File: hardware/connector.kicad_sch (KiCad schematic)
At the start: 6 parts, among them J1 SAFETY_SUPPLY, J2 SWDIO_CONN, J3 SENSORS, J4 VALVES, J5 MAIN, J6 IDC Connector

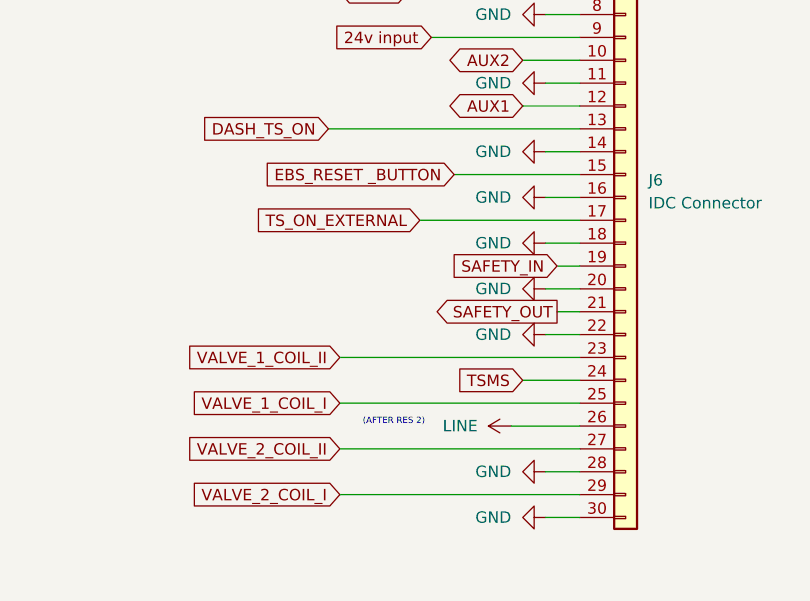
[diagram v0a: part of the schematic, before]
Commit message: replace RES2 input to actuator relai
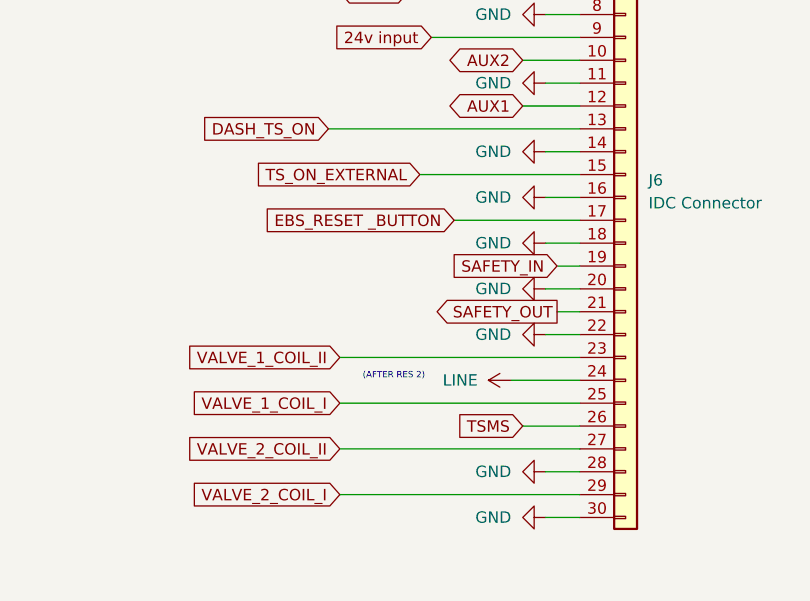
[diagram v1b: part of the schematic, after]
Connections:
- net EBS_RESET _BUTTON: now also J6.17 (Pin_17); no longer J6.15 (Pin_15)
- net LINE: now also J6.24 (Pin_24); no longer J6.26 (Pin_26)
- net TSMS: now also J6.26 (Pin_26); no longer J6.24 (Pin_24)
- net TS_ON_EXTERNAL: now also J6.15 (Pin_15); no longer J6.17 (Pin_17)
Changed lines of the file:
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@@
-    (stroke (width 0) (type default))
-  )
-  (wire (pts (xy 241.3 114.3) (xy 248.92 114.3))
     (stroke (width 0) (type default))
   )
@@
     (stroke (width 0) (type default))
   )
-  (wire (pts (xy 234.95 86.36) (xy 248.92 86.36))
-    (stroke (width 0) (type default))
-  )
-  (wire (pts (xy 231.14 91.44) (xy 248.92 91.44))
-    (stroke (width 0) (type default))
-  )
   (wire (pts (xy 245.11 99.06) (xy 248.92 99.06))
     (stroke (width 0) (type default))
@@
     (stroke (width 0) (type default))
   )
+  (wire (pts (xy 242.57 114.3) (xy 248.92 114.3))
+    (stroke (width 0) (type default))
+  )
   (wire (pts (xy 248.92 81.28) (xy 220.98 81.28))
     (stroke (width 0) (type default))
@@
     (stroke (width 0) (type default))
   )
+  (wire (pts (xy 231.14 86.36) (xy 248.92 86.36))
+    (stroke (width 0) (type default))
+  )
   (wire (pts (xy 245.11 68.58) (xy 248.92 68.58))
     (stroke (width 0) (type default))
@@
     (stroke (width 0) (type default))
   )
-  (wire (pts (xy 242.57 109.22) (xy 248.92 109.22))
+  (wire (pts (xy 241.3 109.22) (xy 248.92 109.22))
     (stroke (width 0) (type default))
   )
@@
   )
   (polyline (pts (xy 143.51 62.23) (xy 143.51 63.5))
+    (stroke (width 0) (type default))
+  )
+  (wire (pts (xy 234.95 91.44) (xy 248.92 91.44))
     (stroke (width 0) (type default))
   )
@@
   (text "HARWIN J-TEK\n" (at 158.75 92.71 0)
     (effects (font (size 1.27 1.27)) (justify left bottom))
-  )
-  (text "(AFTER RES 2)" (at 224.79 114.3 0)
-    (effects (font (size 0.7 0.7)) (justify left bottom))
   )
   (text "Connectors are divided intentionaly- Clue is to speed up inspection process where scrutineer will be unplugging different things and checking functional safety of the system\n"
     (at 49.53 146.05 0)
     (effects (font (size 1.27 1.27) italic) (justify left bottom))
+  )
+  (text "(AFTER RES 2)" (at 224.79 109.22 0)
+    (effects (font (size 0.7 0.7)) (justify left bottom))
   )
   (text "\nM80-5L11242MC\n" (at 161.29 125.73 0)
@@
     )
   )
-  (global_label "EBS_RESET _BUTTON" (shape input) (at 234.95 86.36 180) (fields_autoplaced)
-    (effects (font (size 1.27 1.27)) (justify right))
-    (property "Intersheetrefs" "${INTERSHEET_REFS}" (at 213.0636 86.4394 0)
+  (global_label "TSMS" (shape input) (at 242.57 114.3 180) (fields_autoplaced)
+    (effects (font (size 1.27 1.27)) (justify right))
+    (property "Intersheetrefs" "${INTERSHEET_REFS}" (at 234.8262 114.3 0)
       (effects (font (size 1.27 1.27)) (justify right) hide)
     )
@@
     )
   )
+  (global_label "EBS_RESET _BUTTON" (shape input) (at 234.95 91.44 180) (fields_autoplaced)
+    (effects (font (size 1.27 1.27)) (justify right))
+    (property "Intersheetrefs" "${INTERSHEET_REFS}" (at 213.0636 91.5194 0)
+      (effects (font (size 1.27 1.27)) (justify right) hide)
+    )
+  )
   (global_label "SAFETY_IN" (shape input) (at 246.38 96.52 180) (fields_autoplaced)
     (effects (font (size 1.27 1.27)) (justify right))
@@
     (effects (font (size 1.27 1.27)) (justify right))
     (property "Intersheetrefs" "${INTERSHEET_REFS}" (at 202.7738 53.34 0)
+      (effects (font (size 1.27 1.27)) (justify right) hide)
+    )
+  )
+  (global_label "TS_ON_EXTERNAL" (shape input) (at 231.14 86.36 180) (fields_autoplaced)
+    (effects (font (size 1.27 1.27)) (justify right))
+    (property "Intersheetrefs" "${INTERSHEET_REFS}" (at 212.7612 86.4394 0)
       (effects (font (size 1.27 1.27)) (justify right) hide)
     )
@@
     (effects (font (size 1.27 1.27)) (justify right))
     (property "Intersheetrefs" "${INTERSHEET_REFS}" (at 235.3188 78.6606 0)
-      (effects (font (size 1.27 1.27)) (justify right) hide)
-    )
-  )
-  (global_label "TSMS" (shape input) (at 242.57 109.22 180) (fields_autoplaced)
-    (effects (font (size 1.27 1.27)) (justify right))
-    (property "Intersheetrefs" "${INTERSHEET_REFS}" (at 234.8262 109.22 0)
-      (effects (font (size 1.27 1.27)) (justify right) hide)
-    )
-  )
-  (global_label "TS_ON_EXTERNAL" (shape input) (at 231.14 91.44 180) (fields_autoplaced)
-    (effects (font (size 1.27 1.27)) (justify right))
-    (property "Intersheetrefs" "${INTERSHEET_REFS}" (at 212.7612 91.5194 0)
       (effects (font (size 1.27 1.27)) (justify right) hide)
     )
@@
     )
   )
-  (symbol (lib_id "power:LINE") (at 241.3 114.3 90) (unit 1)
+  (symbol (lib_id "power:LINE") (at 241.3 109.22 90) (unit 1)
     (in_bom yes) (on_board yes) (dnp no)
-    (property "Reference" "#PWR073" (at 245.11 114.3 0)
-      (effects (font (size 1.27 1.27)) hide)
-    )
-    (property "Value" "LINE" (at 233.68 114.3 90)
+    (property "Reference" "#PWR017" (at 245.11 109.22 0)
+      (effects (font (size 1.27 1.27)) hide)
+    )
+    (property "Value" "LINE" (at 233.68 109.22 90)
       (effects (font (size 1.27 1.27)) (justify right))
     )
-    (property "Footprint" "" (at 241.3 114.3 0)
-      (effects (font (size 1.27 1.27)) hide)
-    )
-    (property "Datasheet" "" (at 241.3 114.3 0)
+    (property "Footprint" "" (at 241.3 109.22 0)
+      (effects (font (size 1.27 1.27)) hide)
+    )
+    (property "Datasheet" "" (at 241.3 109.22 0)
       (effects (font (size 1.27 1.27)) hide)
     )
@@
       (project "PUTM_DV_EBS_2023"
         (path "/d921fbb5-521e-405d-bdec-f40195adfa1c/d8688165-16f9-4d4a-b76d-8edb3b6e7c8b"
-          (reference "#PWR073") (unit 1)
+          (reference "#PWR017") (unit 1)
         )
       )

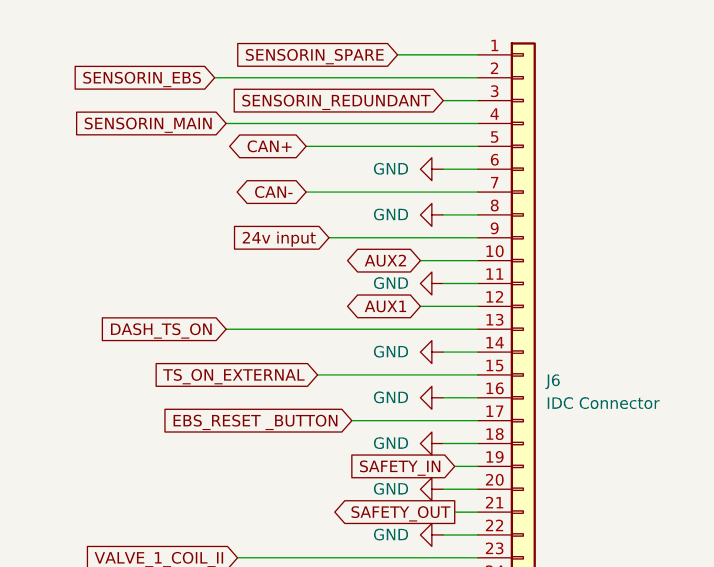
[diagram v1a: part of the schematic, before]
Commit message: Adjust mounting holes to FBOX and BSPD
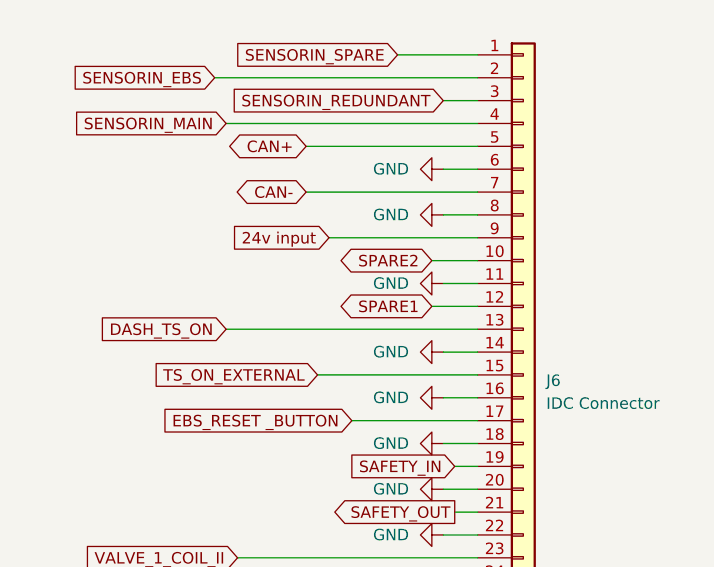
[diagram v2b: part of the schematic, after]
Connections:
- net AUX1 renamed SPARE1
- net AUX2 renamed SPARE2
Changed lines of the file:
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@@
+    (stroke (width 0) (type default))
+  )
+  (wire (pts (xy 248.92 78.74) (xy 243.84 78.74))
     (stroke (width 0) (type default))
   )
@@
     (stroke (width 0) (type default))
   )
-  (wire (pts (xy 248.92 78.74) (xy 242.57 78.74))
-    (stroke (width 0) (type default))
-  )
   (wire (pts (xy 246.38 101.6) (xy 248.92 101.6))
     (stroke (width 0) (type default))
@@
     (stroke (width 0) (type default))
   )
+  (wire (pts (xy 248.92 73.66) (xy 243.84 73.66))
+    (stroke (width 0) (type default))
+  )
   (wire (pts (xy 245.11 99.06) (xy 248.92 99.06))
     (stroke (width 0) (type default))
@@
   )
   (polyline (pts (xy 151.13 87.63) (xy 156.21 87.63))
-    (stroke (width 0) (type default))
-  )
-  (wire (pts (xy 248.92 73.66) (xy 242.57 73.66))
     (stroke (width 0) (type default))
   )
@@
     )
   )
+  (global_label "SPARE1" (shape bidirectional) (at 243.84 78.74 180) (fields_autoplaced)
+    (effects (font (size 1.27 1.27)) (justify right))
+    (property "Intersheetrefs" "${INTERSHEET_REFS}" (at 232.6263 78.74 0)
+      (effects (font (size 1.27 1.27)) (justify right) hide)
+    )
+  )
+  (global_label "SPARE2" (shape bidirectional) (at 243.84 73.66 180) (fields_autoplaced)
+    (effects (font (size 1.27 1.27)) (justify right))
+    (property "Intersheetrefs" "${INTERSHEET_REFS}" (at 232.6263 73.66 0)
+      (effects (font (size 1.27 1.27)) (justify right) hide)
+    )
+  )
   (global_label "CAN+" (shape bidirectional) (at 229.87 60.96 180) (fields_autoplaced)
     (effects (font (size 1.27 1.27)) (justify right))
@@
     )
   )
-  (global_label "AUX2" (shape bidirectional) (at 242.57 73.66 180) (fields_autoplaced)
-    (effects (font (size 1.27 1.27)) (justify right))
-    (property "Intersheetrefs" "${INTERSHEET_REFS}" (at 235.3188 73.5806 0)
-      (effects (font (size 1.27 1.27)) (justify right) hide)
-    )
-  )
   (global_label "SENSORIN_REDUNDANT" (shape input) (at 245.11 55.88 180) (fields_autoplaced)
     (effects (font (size 1.27 1.27)) (justify right))
@@
     )
   )
-  (global_label "AUX1" (shape bidirectional) (at 242.57 78.74 180) (fields_autoplaced)
-    (effects (font (size 1.27 1.27)) (justify right))
-    (property "Intersheetrefs" "${INTERSHEET_REFS}" (at 235.3188 78.6606 0)
-      (effects (font (size 1.27 1.27)) (justify right) hide)
-    )
-  )

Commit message: wip
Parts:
- removed J1: SAFETY_SUPPLY, PUTM_Kicad_FOOTPRINTS:M80-5L104YYMC, symbol Connector_Generic:Conn_01x04
- removed J3: SENSORS, PUTM_Kicad_FOOTPRINTS:M80-5L104YYMC, symbol Connector_Generic:Conn_01x04
- removed J4: VALVES, PUTM_Kicad_FOOTPRINTS:M80-5L104YYMC, symbol Connector_Generic:Conn_01x04
- removed J5: MAIN, PUTM_Kicad_FOOTPRINTS:M80-5L112YYMC, symbol Connector_Generic:Conn_01x12
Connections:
- no-connect marks 3 -> 0
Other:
- note added: "Scrutineering- On the vertical connection board SCS's are routed through jumpers for easy functionality inspection"
- note removed: "10pin version not in stock ;/"
- note removed: "Connectors are divided intentionaly- Clue is to speed up inspection process where scrutineer will be unplugging different things and checking functional safety of the system"
- note removed: "HARWIN J-TEK"
- note removed: "M80-5L10442MC"
- note removed: "M80-5L11242MC"
- note removed: "so they are divided to sections to speed it up"
- moved on the sheet: J6

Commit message: changed pcb version
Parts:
- removed J6: IDC Connector, Connector_IDC:IDC-Header_2x15-1MP_P2.54mm_Latch6.5mm_Vertical, symbol Connector_Generic:Conn_01x30
- added J1: SAFETY_SUPPLY, PUTM_Kicad_FOOTPRINTS:M80-5L104YYMC, symbol Connector_Generic:Conn_01x04
- added J3: SENSORS, PUTM_Kicad_FOOTPRINTS:M80-5L104YYMC, symbol Connector_Generic:Conn_01x04
- added J4: VALVES, PUTM_Kicad_FOOTPRINTS:M80-5L104YYMC, symbol Connector_Generic:Conn_01x04
- added J5: MAIN, PUTM_Kicad_FOOTPRINTS:M80-5L112YYMC, symbol Connector_Generic:Conn_01x12
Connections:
- net 24v input: now also J5.5 (Pin_5)
- net CAN+: now also J5.7 (Pin_7)
- net CAN-: now also J5.1 (Pin_1)
- net DASH_TS_ON: now also J5.2 (Pin_2)
- net EBS_RESET _BUTTON: now also J5.3 (Pin_3)
- net GND: now also J5.6 (Pin_6)
- net LINE: now also J1.3 (Pin_3)
- net SAFETY_IN: now also J1.2 (Pin_2)
- net SAFETY_OUT: now also J1.4 (Pin_4)
- net TS_ON_EXTERNAL: now also J5.8 (Pin_8)
- net VALVE_1_COIL_I: now also J4.1 (Pin_1)
- net VALVE_1_COIL_II: now also J4.3 (Pin_3)
- net VALVE_2_COIL_I: now also J4.2 (Pin_2)
- net VALVE_2_COIL_II: now also J4.4 (Pin_4)
- new net AIR+: J5.12 (Pin_12)
- new net AIR_EBS: J3.3 (Pin_3)
- new net AIR_MAIN: J3.2 (Pin_2)
- new net AIR_REDUNDANT: J3.1 (Pin_1)
- new net AUX1: J5.10 (Pin_10)
- new net AUX2: J5.9 (Pin_9)
- no-connect marks 0 -> 4
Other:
- note added: "10pin version not in stock ;/"
- note added: "Connectors are divided intentionaly- Clue is to speed up inspection process where scrutineer will be unplugging different things and checking functional safety of the system"
- note added: "HARWIN J-TEK"
- note added: "M80-5L10442MC"
- note added: "M80-5L11242MC"
- note added: "so they are divided to sections to speed it up"
- note removed: "Scrutineering- On the vertical connection board SCS's are routed through jumpers for easy functionality inspection"
- moved on the sheet: J2

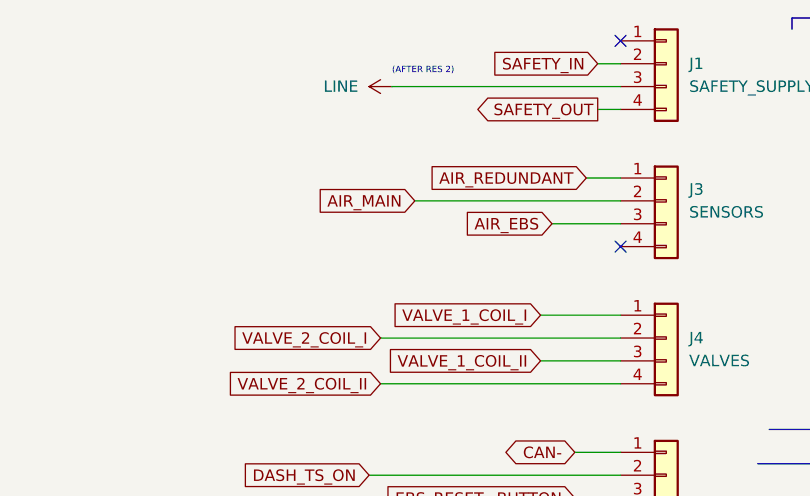
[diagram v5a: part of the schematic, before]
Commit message: Schematic redesign for 23 rules, new pressure buffer, protection fix
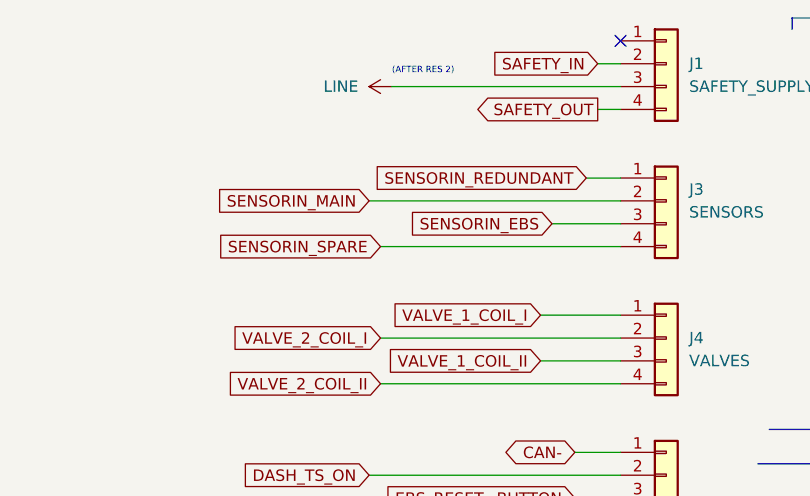
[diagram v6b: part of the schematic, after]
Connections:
- net SENSORIN_SPARE: now reaches J3.4 (Pin_4)
- net AIR_EBS renamed SENSORIN_EBS
- net AIR_MAIN renamed SENSORIN_MAIN
- net AIR_REDUNDANT renamed SENSORIN_REDUNDANT
- no-connect marks 4 -> 3
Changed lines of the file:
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@@
   (no_connect (at 124.46 64.77))
   (no_connect (at 124.46 135.89))
-  (no_connect (at 124.46 87.63))
   (wire (pts (xy 118.11 138.43) (xy 124.46 138.43))
     (stroke (width 0) (type default))
   )
+  (wire (pts (xy 97.79 87.63) (xy 124.46 87.63))
+    (stroke (width 0) (type default))
+  )
   (wire (pts (xy 99.06 69.85) (xy 124.46 69.85))
     (stroke (width 0) (type default))
@@
     (stroke (width 0) (type default))
   )
-  (wire (pts (xy 101.6 82.55) (xy 124.46 82.55))
+  (wire (pts (xy 96.52 82.55) (xy 124.46 82.55))
     (stroke (width 0) (type default))
   )
@@
     )
   )
-  (global_label "AIR_MAIN" (shape input) (at 101.6 82.55 180) (fields_autoplaced)
-    (effects (font (size 1.27 1.27)) (justify right))
-    (property "Intersheetrefs" "${INTERSHEET_REFS}" (at 90.7807 82.4706 0)
-      (effects (font (size 1.27 1.27)) (justify right) hide)
-    )
-  )
   (global_label "AIR+" (shape input) (at 118.11 138.43 180) (fields_autoplaced)
     (effects (font (size 1.27 1.27)) (justify right))
@@
     (effects (font (size 1.27 1.27)) (justify right))
     (property "Intersheetrefs" "${INTERSHEET_REFS}" (at 88.3012 128.3494 0)
+      (effects (font (size 1.27 1.27)) (justify right) hide)
+    )
+  )
+  (global_label "SENSORIN_MAIN" (shape input) (at 96.52 82.55 180) (fields_autoplaced)
+    (effects (font (size 1.27 1.27)) (justify right))
+    (property "Intersheetrefs" "${INTERSHEET_REFS}" (at 78.737 82.55 0)
       (effects (font (size 1.27 1.27)) (justify right) hide)
     )
@@
     )
   )
+  (global_label "SENSORIN_EBS" (shape input) (at 116.84 85.09 180) (fields_autoplaced)
+    (effects (font (size 1.27 1.27)) (justify right))
+    (property "Intersheetrefs" "${INTERSHEET_REFS}" (at 99.9038 85.09 0)
+      (effects (font (size 1.27 1.27)) (justify right) hide)
+    )
+  )
   (global_label "DASH_TS_ON" (shape input) (at 96.52 113.03 180) (fields_autoplaced)
     (effects (font (size 1.27 1.27)) (justify right))
@@
     )
   )
-  (global_label "AIR_EBS" (shape input) (at 116.84 85.09 180) (fields_autoplaced)
-    (effects (font (size 1.27 1.27)) (justify right))
-    (property "Intersheetrefs" "${INTERSHEET_REFS}" (at 106.8674 85.0106 0)
-      (effects (font (size 1.27 1.27)) (justify right) hide)
-    )
-  )
   (global_label "VALVE_2_COIL_II" (shape input) (at 97.79 102.87 180) (fields_autoplaced)
     (effects (font (size 1.27 1.27)) (justify right))
@@
     )
   )
+  (global_label "SENSORIN_REDUNDANT" (shape input) (at 120.65 80.01 180) (fields_autoplaced)
+    (effects (font (size 1.27 1.27)) (justify right))
+    (property "Intersheetrefs" "${INTERSHEET_REFS}" (at 96.3356 80.01 0)
+      (effects (font (size 1.27 1.27)) (justify right) hide)
+    )
+  )
+  (global_label "SENSORIN_SPARE" (shape input) (at 97.79 87.63 180) (fields_autoplaced)
+    (effects (font (size 1.27 1.27)) (justify right))
+    (property "Intersheetrefs" "${INTERSHEET_REFS}" (at 78.4952 87.63 0)
+      (effects (font (size 1.27 1.27)) (justify right) hide)
+    )
+  )
   (global_label "SAFETY_IN" (shape input) (at 121.92 67.31 180) (fields_autoplaced)
     (effects (font (size 1.27 1.27)) (justify right))
@@
       (effects (font (size 1.27 1.27)) (justify right) hide)
     )
-  )
-  (global_label "AIR_REDUNDANT" (shape input) (at 120.65 80.01 180) (fields_autoplaced)
-    (effects (font (size 1.27 1.27)) (justify right))
-    (property "Intersheetrefs" "${INTERSHEET_REFS}" (at 103.2993 79.9306 0)
-      (effects (font (size 1.27 1.27)) (justify right) hide)
-    )

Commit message: WIP revision 2 layout refinement
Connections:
- net AIR+ renamed TSMS
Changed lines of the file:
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@@
     )
   )
-  (global_label "AIR+" (shape input) (at 118.11 138.43 180) (fields_autoplaced)
+  (global_label "TSMS" (shape input) (at 118.11 138.43 180) (fields_autoplaced)
     (effects (font (size 1.27 1.27)) (justify right))
-    (property "Intersheetrefs" "${INTERSHEET_REFS}" (at 111.1612 138.5094 0)
+    (property "Intersheetrefs" "${INTERSHEET_REFS}" (at 110.3662 138.43 0)
       (effects (font (size 1.27 1.27)) (justify right) hide)
     )

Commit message: 2.0 layot wip , routing 3
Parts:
- added J6: IDC Connector, Connector_IDC:IDC-Header_2x15-1MP_P2.54mm_Latch6.5mm_Vertical, symbol Connector_Generic:Conn_01x30
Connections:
- net 24v input: now also J6.9 (Pin_9); no longer J5.5 (Pin_5)
- net AUX1: now also J6.12 (Pin_12); no longer J5.10 (Pin_10)
- net AUX2: now also J6.10 (Pin_10); no longer J5.9 (Pin_9)
- net CAN+: now also J6.5 (Pin_5); no longer J5.7 (Pin_7)
- net CAN-: now also J6.7 (Pin_7); no longer J5.1 (Pin_1)
- net DASH_TS_ON: now also J6.13 (Pin_13); no longer J5.2 (Pin_2)
- net EBS_RESET _BUTTON: now also J6.15 (Pin_15); no longer J5.3 (Pin_3)
- net GND: now also J6.11 (Pin_11), J6.14 (Pin_14), J6.16 (Pin_16), J6.18 (Pin_18), J6.20 (Pin_20), J6.22 (Pin_22), J6.28 (Pin_28), J6.30 (Pin_30), J6.6 (Pin_6), J6.8 (Pin_8); no longer J5.6 (Pin_6)
- net LINE: now also J6.26 (Pin_26); no longer J1.3 (Pin_3)
- net SAFETY_IN: now also J6.19 (Pin_19); no longer J1.2 (Pin_2)
- net SAFETY_OUT: now also J6.21 (Pin_21); no longer J1.4 (Pin_4)
- net SENSORIN_EBS: now also J6.2 (Pin_2); no longer J3.3 (Pin_3)
- net SENSORIN_MAIN: now also J6.4 (Pin_4); no longer J3.2 (Pin_2)
- net SENSORIN_REDUNDANT: now also J6.3 (Pin_3); no longer J3.1 (Pin_1)
- net SENSORIN_SPARE: now also J6.1 (Pin_1); no longer J3.4 (Pin_4)
- net TSMS: now also J6.24 (Pin_24); no longer J5.12 (Pin_12)
- net TS_ON_EXTERNAL: now also J6.17 (Pin_17); no longer J5.8 (Pin_8)
- net VALVE_1_COIL_I: now also J6.25 (Pin_25); no longer J4.1 (Pin_1)
- net VALVE_1_COIL_II: now also J6.23 (Pin_23); no longer J4.3 (Pin_3)
- net VALVE_2_COIL_I: now also J6.29 (Pin_29); no longer J4.2 (Pin_2)
- net VALVE_2_COIL_II: now also J6.27 (Pin_27); no longer J4.4 (Pin_4)
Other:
- moved on the sheet: J2
